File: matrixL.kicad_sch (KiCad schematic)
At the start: 66 parts, among them SW1 SW_Push, SW10 SW_Push, SW11 SW_Push, SW12 SW_Push, SW13 SW_Push, SW14 SW_Push, SW15 SW_Push, SW16 SW_Push, SW17 SW_Push, SW18 SW_Push, SW19 SW_Push, SW2 SW_Push, SW20 SW_Push, SW21 SW_Push, SW22 SW_Push, SW23 SW_Push, SW24 SW_Push, SW25 SW_Push, SW26 SW_Push, SW27 SW_Push, SW28 SW_Push, SW29 SW_Push, SW3 SW_Push, SW30 SW_Push, SW31 SW_Push, SW32 SW_Push, SW33 SW_Push, SW4 SW_Push, SW5 SW_Push, SW6 SW_Push, SW7 SW_Push, SW8 SW_Push, SW9 SW_Push

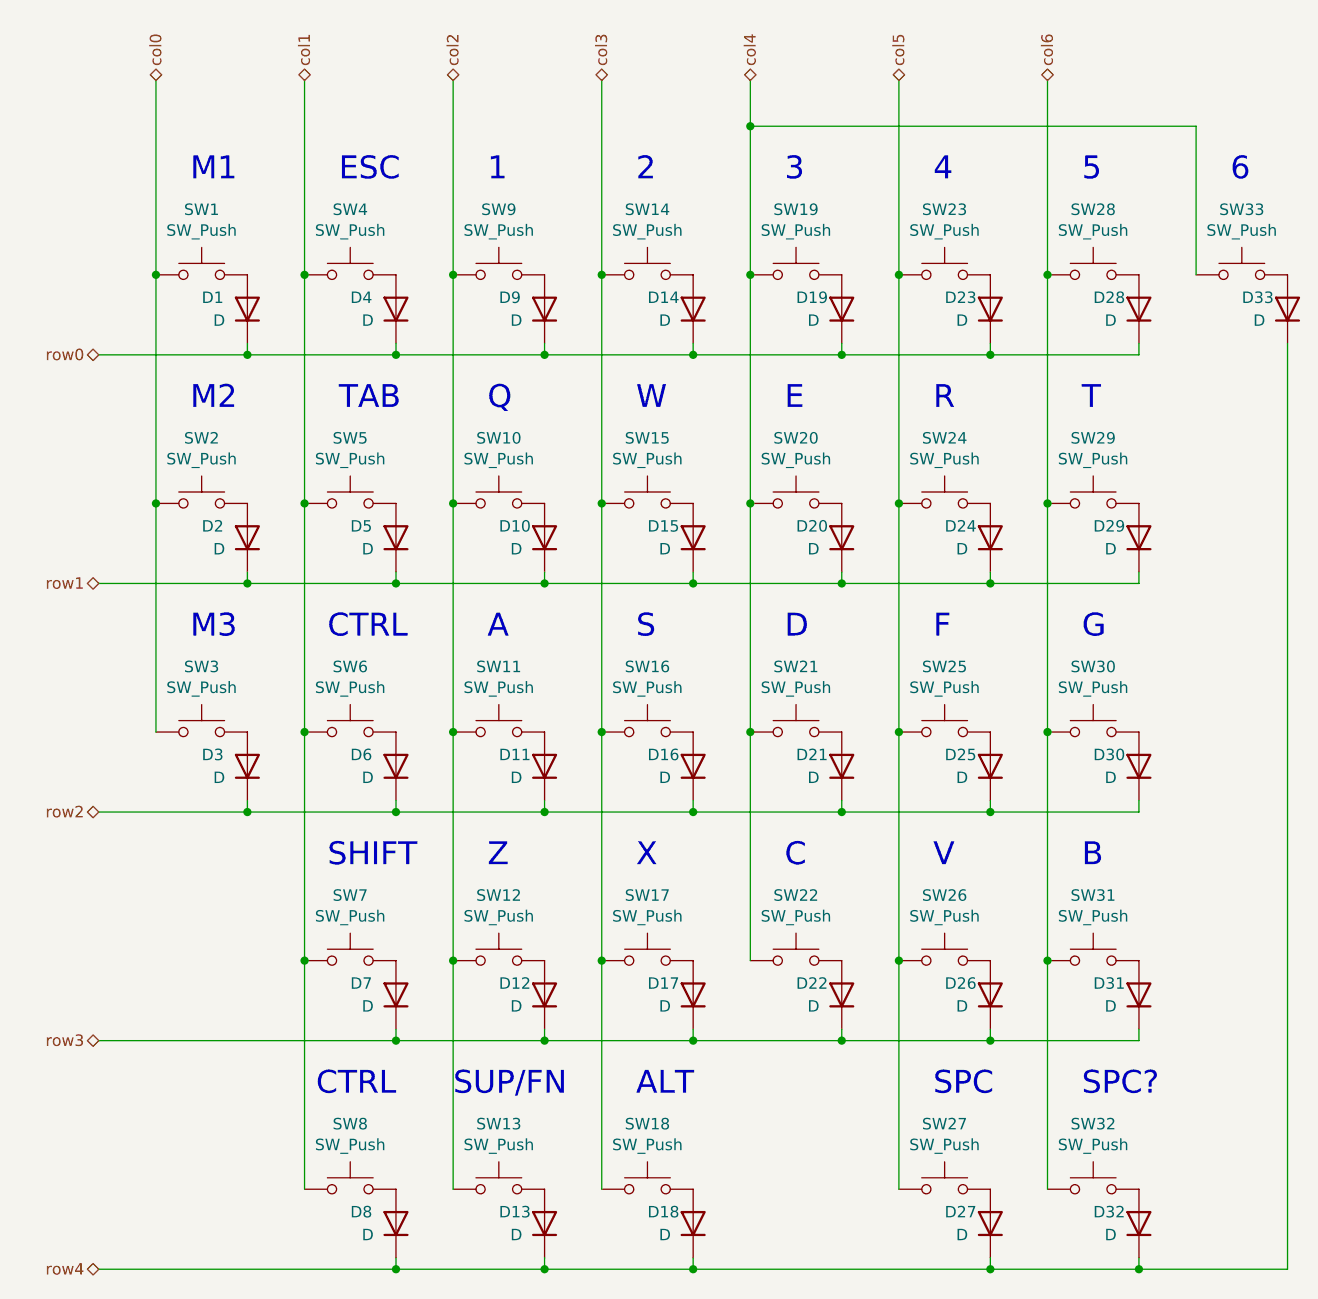
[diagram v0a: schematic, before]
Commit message: Hot pluggable trrs
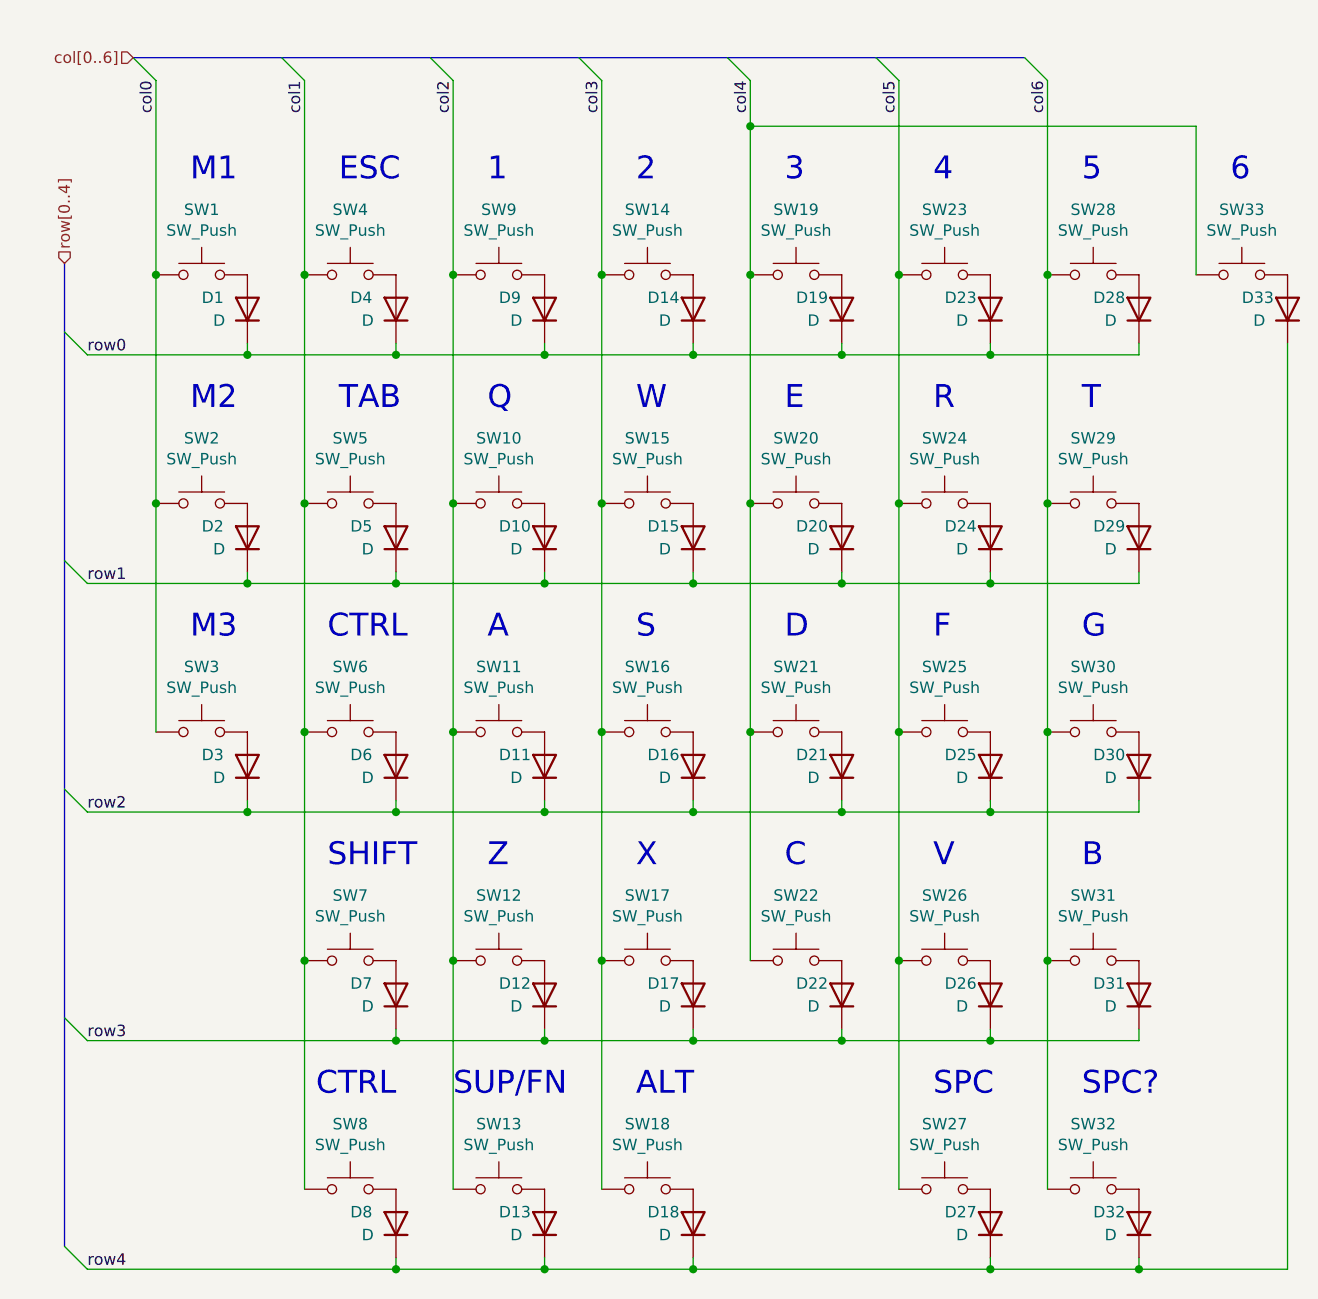
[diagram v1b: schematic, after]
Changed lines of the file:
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@@
   (junction (at 48.26 124.46) (diameter 0) (color 0 0 0 0)
   )
+  (bus_entry (at 29.21 24.13) (size 2.54 2.54)
+    (stroke (width 0) (type default) (color 0 0 0 0))
+  )
+  (bus_entry (at 21.59 80.01) (size 2.54 2.54)
+    (stroke (width 0) (type default) (color 0 0 0 0))
+  )
+  (bus_entry (at 111.76 24.13) (size 2.54 2.54)
+    (stroke (width 0) (type default) (color 0 0 0 0))
+  )
+  (bus_entry (at 62.23 24.13) (size 2.54 2.54)
+    (stroke (width 0) (type default) (color 0 0 0 0))
+  )
+  (bus_entry (at 95.25 24.13) (size 2.54 2.54)
+    (stroke (width 0) (type default) (color 0 0 0 0))
+  )
+  (bus_entry (at 21.59 105.41) (size 2.54 2.54)
+    (stroke (width 0) (type default) (color 0 0 0 0))
+  )
+  (bus_entry (at 21.59 54.61) (size 2.54 2.54)
+    (stroke (width 0) (type default) (color 0 0 0 0))
+  )
+  (bus_entry (at 21.59 156.21) (size 2.54 2.54)
+    (stroke (width 0) (type default) (color 0 0 0 0))
+  )
+  (bus_entry (at 21.59 130.81) (size 2.54 2.54)
+    (stroke (width 0) (type default) (color 0 0 0 0))
+  )
+  (bus_entry (at 45.72 24.13) (size 2.54 2.54)
+    (stroke (width 0) (type default) (color 0 0 0 0))
+  )
+  (bus_entry (at 78.74 24.13) (size 2.54 2.54)
+    (stroke (width 0) (type default) (color 0 0 0 0))
+  )
+  (bus_entry (at 128.27 24.13) (size 2.54 2.54)
+    (stroke (width 0) (type default) (color 0 0 0 0))
+  )
   (wire (pts (xy 97.79 48.26) (xy 97.79 73.66))
     (stroke (width 0) (type default) (color 0 0 0 0))
@@
     (stroke (width 0) (type default) (color 0 0 0 0))
   )
+  (bus (pts (xy 21.59 130.81) (xy 21.59 156.21))
+    (stroke (width 0) (type default) (color 0 0 0 0))
+  )
   (wire (pts (xy 97.79 31.75) (xy 147.32 31.75))
     (stroke (width 0) (type default) (color 0 0 0 0))
@@
     (stroke (width 0) (type default) (color 0 0 0 0))
   )
+  (bus (pts (xy 111.76 24.13) (xy 128.27 24.13))
+    (stroke (width 0) (type default) (color 0 0 0 0))
+  )
   (wire (pts (xy 58.42 81.28) (xy 58.42 82.55))
     (stroke (width 0) (type default) (color 0 0 0 0))
@@
     (stroke (width 0) (type default) (color 0 0 0 0))
   )
+  (bus (pts (xy 78.74 24.13) (xy 95.25 24.13))
+    (stroke (width 0) (type default) (color 0 0 0 0))
+  )
   (wire (pts (xy 64.77 99.06) (xy 64.77 124.46))
     (stroke (width 0) (type default) (color 0 0 0 0))
@@
     (stroke (width 0) (type default) (color 0 0 0 0))
   )
-  (wire (pts (xy 25.4 82.55) (xy 41.91 82.55))
+  (wire (pts (xy 24.13 82.55) (xy 41.91 82.55))
     (stroke (width 0) (type default) (color 0 0 0 0))
   )
@@
     (stroke (width 0) (type default) (color 0 0 0 0))
   )
+  (bus (pts (xy 21.59 80.01) (xy 21.59 105.41))
+    (stroke (width 0) (type default) (color 0 0 0 0))
+  )
   (wire (pts (xy 48.26 124.46) (xy 48.26 149.86))
     (stroke (width 0) (type default) (color 0 0 0 0))
@@
     (stroke (width 0) (type default) (color 0 0 0 0))
   )
+  (bus (pts (xy 29.21 24.13) (xy 45.72 24.13))
+    (stroke (width 0) (type default) (color 0 0 0 0))
+  )
   (wire (pts (xy 140.97 158.75) (xy 157.48 158.75))
     (stroke (width 0) (type default) (color 0 0 0 0))
@@
     (stroke (width 0) (type default) (color 0 0 0 0))
   )
+  (bus (pts (xy 21.59 54.61) (xy 21.59 80.01))
+    (stroke (width 0) (type default) (color 0 0 0 0))
+  )
   (wire (pts (xy 97.79 31.75) (xy 97.79 48.26))
     (stroke (width 0) (type default) (color 0 0 0 0))
@@
     (stroke (width 0) (type default) (color 0 0 0 0))
   )
-  (wire (pts (xy 25.4 158.75) (xy 58.42 158.75))
+  (wire (pts (xy 24.13 158.75) (xy 58.42 158.75))
     (stroke (width 0) (type default) (color 0 0 0 0))
   )
@@
     (stroke (width 0) (type default) (color 0 0 0 0))
   )
+  (bus (pts (xy 45.72 24.13) (xy 62.23 24.13))
+    (stroke (width 0) (type default) (color 0 0 0 0))
+  )
   (wire (pts (xy 114.3 124.46) (xy 114.3 149.86))
     (stroke (width 0) (type default) (color 0 0 0 0))
@@
     (stroke (width 0) (type default) (color 0 0 0 0))
   )
-  (wire (pts (xy 25.4 107.95) (xy 41.91 107.95))
+  (wire (pts (xy 24.13 107.95) (xy 41.91 107.95))
     (stroke (width 0) (type default) (color 0 0 0 0))
   )
@@
     (stroke (width 0) (type default) (color 0 0 0 0))
   )
+  (bus (pts (xy 95.25 24.13) (xy 111.76 24.13))
+    (stroke (width 0) (type default) (color 0 0 0 0))
+  )
   (wire (pts (xy 74.93 81.28) (xy 74.93 82.55))
     (stroke (width 0) (type default) (color 0 0 0 0))
@@
     (stroke (width 0) (type default) (color 0 0 0 0))
   )
-  (wire (pts (xy 25.4 133.35) (xy 58.42 133.35))
-    (stroke (width 0) (type default) (color 0 0 0 0))
-  )
-  (wire (pts (xy 25.4 57.15) (xy 41.91 57.15))
+  (wire (pts (xy 24.13 133.35) (xy 58.42 133.35))
+    (stroke (width 0) (type default) (color 0 0 0 0))
+  )
+  (wire (pts (xy 24.13 57.15) (xy 41.91 57.15))
     (stroke (width 0) (type default) (color 0 0 0 0))
   )
@@
     (stroke (width 0) (type default) (color 0 0 0 0))
   )
+  (bus (pts (xy 62.23 24.13) (xy 78.74 24.13))
+    (stroke (width 0) (type default) (color 0 0 0 0))
+  )
   (wire (pts (xy 48.26 73.66) (xy 48.26 99.06))
     (stroke (width 0) (type default) (color 0 0 0 0))
@@
     (stroke (width 0) (type default) (color 0 0 0 0))
   )
+  (bus (pts (xy 21.59 105.41) (xy 21.59 130.81))
+    (stroke (width 0) (type default) (color 0 0 0 0))
+  )
   (wire (pts (xy 91.44 82.55) (xy 107.95 82.55))
     (stroke (width 0) (type default) (color 0 0 0 0))
   )
+  (bus (pts (xy 21.59 46.99) (xy 21.59 54.61))
+    (stroke (width 0) (type default) (color 0 0 0 0))
+  )
   (wire (pts (xy 81.28 26.67) (xy 81.28 48.26))
     (stroke (width 0) (type default) (color 0 0 0 0))
@@
     (effects (font (size 2.54 2.54)) (justify left bottom))
   )
-  (hierarchical_label "col4" (shape tri_state) (at 97.79 26.67 90)
+  (label "col4" (at 97.79 26.67 270)
+    (effects (font (size 1.27 1.27)) (justify right bottom))
+  )
+  (label "row3" (at 24.13 133.35 0)
+    (effects (font (size 1.27 1.27)) (justify left bottom))
+  )
+  (label "row4" (at 24.13 158.75 0)
+    (effects (font (size 1.27 1.27)) (justify left bottom))
+  )
+  (label "col5" (at 114.3 26.67 270)
+    (effects (font (size 1.27 1.27)) (justify right bottom))
+  )
+  (label "row1" (at 24.13 82.55 0)
+    (effects (font (size 1.27 1.27)) (justify left bottom))
+  )
+  (label "row0" (at 24.13 57.15 0)
+    (effects (font (size 1.27 1.27)) (justify left bottom))
+  )
+  (label "col3" (at 81.28 26.67 270)
+    (effects (font (size 1.27 1.27)) (justify right bottom))
+  )
+  (label "col2" (at 64.77 26.67 270)
+    (effects (font (size 1.27 1.27)) (justify right bottom))
+  )
+  (label "col1" (at 48.26 26.67 270)
+    (effects (font (size 1.27 1.27)) (justify right bottom))
+  )
+  (label "col0" (at 31.75 26.67 270)
+    (effects (font (size 1.27 1.27)) (justify right bottom))
+  )
+  (label "col6" (at 130.81 26.67 270)
+    (effects (font (size 1.27 1.27)) (justify right bottom))
+  )
+  (label "row2" (at 24.13 107.95 0)
+    (effects (font (size 1.27 1.27)) (justify left bottom))
+  )
+  (hierarchical_label "col[0..6]" (shape input) (at 29.21 24.13 180)
+    (effects (font (size 1.27 1.27)) (justify right))
+  )
+  (hierarchical_label "row[0..4]" (shape input) (at 21.59 46.99 90)
     (effects (font (size 1.27 1.27)) (justify left))
   )
-  (hierarchical_label "col0" (shape tri_state) (at 31.75 26.67 90)
-    (effects (font (size 1.27 1.27)) (justify left))
-  )
-  (hierarchical_label "col3" (shape tri_state) (at 81.28 26.67 90)
-    (effects (font (size 1.27 1.27)) (justify left))
-  )
-  (hierarchical_label "row1" (shape tri_state) (at 25.4 82.55 180)
-    (effects (font (size 1.27 1.27)) (justify right))
-  )
-  (hierarchical_label "col2" (shape tri_state) (at 64.77 26.67 90)
-    (effects (font (size 1.27 1.27)) (justify left))
-  )
-  (hierarchical_label "row4" (shape tri_state) (at 25.4 158.75 180)
-    (effects (font (size 1.27 1.27)) (justify right))
-  )
-  (hierarchical_label "col1" (shape tri_state) (at 48.26 26.67 90)
-    (effects (font (size 1.27 1.27)) (justify left))
-  )
-  (hierarchical_label "row2" (shape tri_state) (at 25.4 107.95 180)
-    (effects (font (size 1.27 1.27)) (justify right))
-  )
-  (hierarchical_label "row3" (shape tri_state) (at 25.4 133.35 180)
-    (effects (font (size 1.27 1.27)) (justify right))
-  )
-  (hierarchical_label "row0" (shape tri_state) (at 25.4 57.15 180)
-    (effects (font (size 1.27 1.27)) (justify right))
-  )
-  (hierarchical_label "col5" (shape tri_state) (at 114.3 26.67 90)
-    (effects (font (size 1.27 1.27)) (justify left))
-  )
-  (hierarchical_label "col6" (shape tri_state) (at 130.81 26.67 90)
-    (effects (font (size 1.27 1.27)) (justify left))
-  )

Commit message: No more erc errors + centering and socketing of switches
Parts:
- SW1, SW10, SW11, SW12, SW14, SW15, SW16, SW17, SW19, SW2, SW20, SW21, SW22, SW23, SW24, SW25, SW26, SW28, SW29, SW3, SW30, SW31, SW32, SW33, SW4, SW9: footprint MX_Switch:SW_Cherry_MX_1.00u_PCB -> MX_Switch:SW_Cherry_MX_1.00u_PCB_Socket
- SW13, SW18, SW5, SW8: footprint MX_Switch:SW_Cherry_MX_1.50u_PCB -> MX_Switch:SW_Cherry_MX_1.50u_PCB_Socket
- SW27: footprint MX_Switch:SW_Cherry_MX_2.00u_PCB_ReversedStabilizers -> MX_Switch:SW_Cherry_MX_2.00u_PCB_Socket_ReversedStabilizers
- SW6: footprint MX_Switch:SW_Cherry_MX_1.75u_PCB -> MX_Switch:SW_Cherry_MX_1.75u_PCB_Socket
- SW7: footprint MX_Switch:SW_Cherry_MX_2.25u_PCB -> MX_Switch:SW_Cherry_MX_2.25u_PCB_Socket_ReversedStabilizers
